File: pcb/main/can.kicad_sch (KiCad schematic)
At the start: 2 parts

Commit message: chore: add circuit git changes
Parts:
- removed R?: R_Small, symbol Device:R_Small
- removed U?: MCP2562-E-SN, Package_SO:SOIC-8_3.9x4.9mm_P1.27mm, symbol Interface_CAN_LIN:MCP2562-E-SN
- added J10, J8, J9: Conn, bldc_lib:21322604YY, symbol Connector_Generic:Conn_01x06
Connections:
- net +5V: now also J10.1 (Pin_1), J8.1 (Pin_1), J9.1 (Pin_1)
- net CAN_H: now also J10.3 (Pin_3), J8.3 (Pin_3), J9.3 (Pin_3)
- net CAN_L: now also J10.2 (Pin_2), J8.2 (Pin_2), J9.2 (Pin_2)
- net GND: now also J10.4 (Pin_4), J10.5 (Pin_5), J10.6 (Pin_6), J8.4 (Pin_4), J8.5 (Pin_5), J8.6 (Pin_6), J9.4 (Pin_4), J9.5 (Pin_5), J9.6 (Pin_6)
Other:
- removed sheet can1_1
- removed sheet can1_2
- removed sheet can1_3

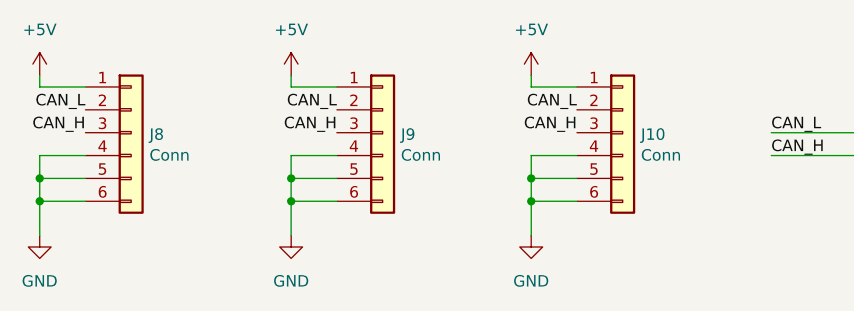
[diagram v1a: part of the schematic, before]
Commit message: perf: update LCD and microSD
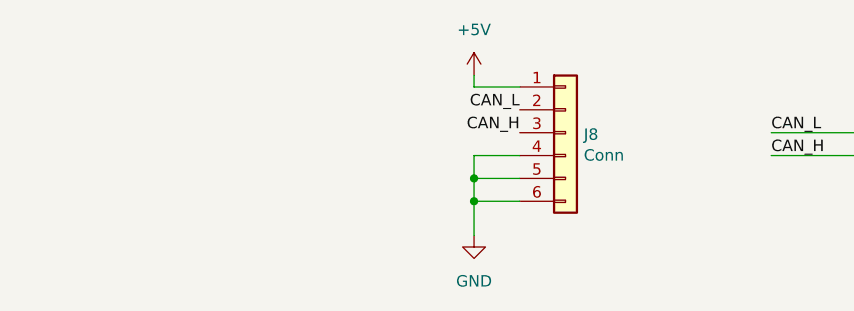
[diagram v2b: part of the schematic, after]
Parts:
- removed J10, J9: Conn, bldc_lib:21322604YY, symbol Connector_Generic:Conn_01x06
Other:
- moved on the sheet: J8
